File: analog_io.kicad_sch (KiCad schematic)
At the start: 12 parts, among them CN2 MX15EDGRHC-3.5-2*02P-BK01-CU-A, U8 ADS1115IDGS

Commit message: Checkpoint: RA5 base board finished, M.2 shield interconnect defined
Base board (ra5_2022):
- Finalize component placement on ra5_2022.kicad_pcb; next step is routing
- Add STM8S003F3P to bridge the 2 digital inputs / 2 digital outputs onto
  the shared I2C bus (alongside the ADS1115), freeing up M.2 pins
- Wire J1 (M.2 Key-E) to a custom, non-spec-compliant 3.3V pinout: I2C
  (SDA/SCL/ALERT#) on the native pins, M90E32AS SPI reusing the SD/SDIO
  "SPI mode" pin convention (SCLK/MOSI/MISO/CS), PM0/PM1 on VENDOR_DEFINED
  pins, USB-C passthrough, full GND/VDD
- Fix AS0BC21-S40BE-7H footprint: pads 76/77 (shield/ground tabs, not part
  of the 75-pin M.2 spec) remapped onto the GND pin instead of dangling
- Swap the buck inductor (L2) for SLW5040S100MST (C182189): same 10uH,
  lower DCR, 5x5mm footprint to clear a routing constraint
- Remove the unused "Production" KiCad Design Variant and align the
  remaining "Develop" variant's footprints with the defaults -- a
  variant/default footprint mismatch was causing Update PCB from Schematic
  to silently duplicate footprints on every sync
- Clean up 10 further orphaned duplicate footprints left on the PCB from
  earlier design revisions (R11, R12, C14, C16, C17, C18, C29, C31, C32, C35)
- Fix 3D model paths across the shared library to use the RA5_2022_LIB
  environment variable instead of ${KIPRJMOD}, so previews resolve
  correctly from sibling projects too

New sibling project (ra5_shield_modem/):
- MCU + LTE modem card, built to the M.2 Key-E mechanical form factor to
  plug into the base board's J1
- Share the ra5_2022 parts library via sym-lib-table/fp-lib-table
- Add the timonsku/M.2-Card-Footprints submodule as a card-edge template

Co-Authored-By: Claude Sonnet 5 <noreply@anthropic.com>
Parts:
- renumbered C31 to C38, C32 to C39, C35 to C40, D17 to D7, D18 to D8, R57 to R55, R58 to R56, R59 to R57, R60 to R58, R61 to R59, U8 to U12
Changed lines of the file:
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@@
 		(in_pos_files yes)
 		(dnp no)
-		(property "Reference" "C32"
+		(property "Reference" "C39"
 			(at 196.596 76.2 0)
 			(show_name no)
@@
 			(project "ra5_2022"
 				(path "/5cbb1e83-2d68-46fe-9857-942ec50591ae/452b8f5a-797d-4028-91e0-40fe10fe98ae/5bd1a3d1-53b1-46ae-9d95-ca4bdd3c4887"
-					(reference "C32")
+					(reference "C39")
 					(unit 1)
 					(variant
 						(name "Develop")
-					)
-					(variant
-						(name "Production")
 					)
 				)
@@
 		(dnp no)
 		(fields_autoplaced yes)
-		(property "Reference" "#PWR074"
+		(property "Reference" "#PWR080"
 			(at 44.45 59.69 0)
 			(hide yes)
@@
 			(project "ra5_2022"
 				(path "/5cbb1e83-2d68-46fe-9857-942ec50591ae/452b8f5a-797d-4028-91e0-40fe10fe98ae/5bd1a3d1-53b1-46ae-9d95-ca4bdd3c4887"
-					(reference "#PWR074")
+					(reference "#PWR080")
 					(unit 1)
 				)
@@
 		(dnp no)
 		(fields_autoplaced yes)
-		(property "Reference" "R61"
+		(property "Reference" "R59"
 			(at 184.15 104.1399 0)
 			(show_name no)
@@
 			(project "ra5_2022"
 				(path "/5cbb1e83-2d68-46fe-9857-942ec50591ae/452b8f5a-797d-4028-91e0-40fe10fe98ae/5bd1a3d1-53b1-46ae-9d95-ca4bdd3c4887"
-					(reference "R61")
+					(reference "R59")
 					(unit 1)
 					(variant
 						(name "Develop")
-					)
-					(variant
-						(name "Production")
 					)
 				)
@@
 		(dnp no)
 		(fields_autoplaced yes)
-		(property "Reference" "#PWR079"
+		(property "Reference" "#PWR086"
 			(at 128.27 109.22 0)
 			(hide yes)
@@
 			(project "ra5_2022"
 				(path "/5cbb1e83-2d68-46fe-9857-942ec50591ae/452b8f5a-797d-4028-91e0-40fe10fe98ae/5bd1a3d1-53b1-46ae-9d95-ca4bdd3c4887"
-					(reference "#PWR079")
+					(reference "#PWR086")
 					(unit 1)
 				)
@@
 		(dnp no)
 		(fields_autoplaced yes)
-		(property "Reference" "U8"
+		(property "Reference" "U12"
 			(at 130.4133 77.47 0)
 			(show_name no)
@@
 			(project "ra5_2022"
 				(path "/5cbb1e83-2d68-46fe-9857-942ec50591ae/452b8f5a-797d-4028-91e0-40fe10fe98ae/5bd1a3d1-53b1-46ae-9d95-ca4bdd3c4887"
-					(reference "U8")
+					(reference "U12")
 					(unit 1)
 					(variant
 						(name "Develop")
-					)
-					(variant
-						(name "Production")
 					)
 				)
@@
 		(dnp no)
 		(fields_autoplaced yes)
-		(property "Reference" "D17"
+		(property "Reference" "D7"
 			(at 171.7675 62.23 0)
 			(show_name no)
@@
 			(project "ra5_2022"
 				(path "/5cbb1e83-2d68-46fe-9857-942ec50591ae/452b8f5a-797d-4028-91e0-40fe10fe98ae/5bd1a3d1-53b1-46ae-9d95-ca4bdd3c4887"
-					(reference "D17")
+					(reference "D7")
 					(unit 1)
 					(variant
 						(name "Develop")
-					)
-					(variant
-						(name "Production")
 					)
 				)
@@
 		(in_pos_files yes)
 		(dnp no)
-		(property "Reference" "R59"
+		(property "Reference" "R57"
 			(at 66.802 60.96 0)
 			(show_name no)
@@
 			(project "ra5_2022"
 				(path "/5cbb1e83-2d68-46fe-9857-942ec50591ae/452b8f5a-797d-4028-91e0-40fe10fe98ae/5bd1a3d1-53b1-46ae-9d95-ca4bdd3c4887"
-					(reference "R59")
+					(reference "R57")
 					(unit 1)
 					(variant
 						(name "Develop")
-					)
-					(variant
-						(name "Production")
 					)
 				)
@@
 		(dnp no)
 		(fields_autoplaced yes)
-		(property "Reference" "#PWR078"
+		(property "Reference" "#PWR084"
 			(at 76.2 74.93 0)
 			(hide yes)
@@
 			(project "ra5_2022"
 				(path "/5cbb1e83-2d68-46fe-9857-942ec50591ae/452b8f5a-797d-4028-91e0-40fe10fe98ae/5bd1a3d1-53b1-46ae-9d95-ca4bdd3c4887"
-					(reference "#PWR078")
+					(reference "#PWR084")
 					(unit 1)
 				)
@@
 		(dnp no)
 		(fields_autoplaced yes)
-		(property "Reference" "#PWR092"
+		(property "Reference" "#PWR085"
 			(at 128.27 83.82 0)
 			(hide yes)
@@
 			(project "ra5_2022"
 				(path "/5cbb1e83-2d68-46fe-9857-942ec50591ae/452b8f5a-797d-4028-91e0-40fe10fe98ae/5bd1a3d1-53b1-46ae-9d95-ca4bdd3c4887"
-					(reference "#PWR092")
+					(reference "#PWR085")
 					(unit 1)
 				)
@@
 		(in_pos_files yes)
 		(dnp no)
-		(property "Reference" "C35"
+		(property "Reference" "C40"
 			(at 196.596 106.68 0)
 			(show_name no)
@@
 			(project "ra5_2022"
 				(path "/5cbb1e83-2d68-46fe-9857-942ec50591ae/452b8f5a-797d-4028-91e0-40fe10fe98ae/5bd1a3d1-53b1-46ae-9d95-ca4bdd3c4887"
-					(reference "C35")
+					(reference "C40")
 					(unit 1)
 					(variant
 						(name "Develop")
-					)
-					(variant
-						(name "Production")
 					)
 				)
@@
 		(dnp no)
 		(fields_autoplaced yes)
-		(property "Reference" "#PWR076"
+		(property "Reference" "#PWR082"
 			(at 63.5 59.69 0)
 			(hide yes)
@@
 			(project "ra5_2022"
 				(path "/5cbb1e83-2d68-46fe-9857-942ec50591ae/452b8f5a-797d-4028-91e0-40fe10fe98ae/5bd1a3d1-53b1-46ae-9d95-ca4bdd3c4887"
-					(reference "#PWR076")
+					(reference "#PWR082")
 					(unit 1)
 				)
@@
 		(dnp no)
 		(fields_autoplaced yes)
-		(property "Reference" "D18"
+		(property "Reference" "D8"
 			(at 171.7675 92.71 0)
 			(show_name no)
@@
 			(project "ra5_2022"
 				(path "/5cbb1e83-2d68-46fe-9857-942ec50591ae/452b8f5a-797d-4028-91e0-40fe10fe98ae/5bd1a3d1-53b1-46ae-9d95-ca4bdd3c4887"
-					(reference "D18")
+					(reference "D8")
 					(unit 1)
 					(variant
 						(name "Develop")
-					)
-					(variant
-						(name "Production")
 					)
 				)
@@
 						(name "Develop")
 					)
-					(variant
-						(name "Production")
-					)
 				)
 			)
@@
 		(dnp no)
 		(fields_autoplaced yes)
-		(property "Reference" "#PWR075"
+		(property "Reference" "#PWR081"
 			(at 54.61 59.69 0)
 			(hide yes)
@@
 			(project "ra5_2022"
 				(path "/5cbb1e83-2d68-46fe-9857-942ec50591ae/452b8f5a-797d-4028-91e0-40fe10fe98ae/5bd1a3d1-53b1-46ae-9d95-ca4bdd3c4887"
-					(reference "#PWR075")
+					(reference "#PWR081")
 					(unit 1)
 				)
@@
 		(in_pos_files yes)
 		(dnp no)
-		(property "Reference" "R58"
+		(property "Reference" "R56"
 			(at 57.912 60.96 0)
 			(show_name no)
@@
 			(project "ra5_2022"
 				(path "/5cbb1e83-2d68-46fe-9857-942ec50591ae/452b8f5a-797d-4028-91e0-40fe10fe98ae/5bd1a3d1-53b1-46ae-9d95-ca4bdd3c4887"
-					(reference "R58")
+					(reference "R56")
 					(unit 1)
 					(variant
 						(name "Develop")
-					)
-					(variant
-						(name "Production")
 					)
 				)
@@
 		(dnp no)
 		(fields_autoplaced yes)
-		(property "Reference" "#PWR091"
+		(property "Reference" "#PWR087"
 			(at 138.43 104.14 0)
 			(hide yes)
@@
 			(project "ra5_2022"
 				(path "/5cbb1e83-2d68-46fe-9857-942ec50591ae/452b8f5a-797d-4028-91e0-40fe10fe98ae/5bd1a3d1-53b1-46ae-9d95-ca4bdd3c4887"
-					(reference "#PWR091")
+					(reference "#PWR087")
 					(unit 1)
 				)
@@
 		(in_pos_files yes)
 		(dnp no)
-		(property "Reference" "R57"
+		(property "Reference" "R55"
 			(at 47.752 60.96 0)
 			(show_name no)
@@
 			(project "ra5_2022"
 				(path "/5cbb1e83-2d68-46fe-9857-942ec50591ae/452b8f5a-797d-4028-91e0-40fe10fe98ae/5bd1a3d1-53b1-46ae-9d95-ca4bdd3c4887"
-					(reference "R57")
+					(reference "R55")
 					(unit 1)
 					(variant
 						(name "Develop")
-					)
-					(variant
-						(name "Production")
 					)
 				)
@@
 		(dnp no)
 		(fields_autoplaced yes)
-		(property "Reference" "#PWR077"
+		(property "Reference" "#PWR083"
 			(at 76.2 59.69 0)
 			(hide yes)
@@
 			(project "ra5_2022"
 				(path "/5cbb1e83-2d68-46fe-9857-942ec50591ae/452b8f5a-797d-4028-91e0-40fe10fe98ae/5bd1a3d1-53b1-46ae-9d95-ca4bdd3c4887"
-					(reference "#PWR077")
+					(reference "#PWR083")
 					(unit 1)
 				)
@@
 		(in_pos_files yes)
 		(dnp no)
-		(property "Reference" "C31"
+		(property "Reference" "C38"
 			(at 79.756 63.5 0)
 			(show_name no)
@@
 			(project "ra5_2022"
 				(path "/5cbb1e83-2d68-46fe-9857-942ec50591ae/452b8f5a-797d-4028-91e0-40fe10fe98ae/5bd1a3d1-53b1-46ae-9d95-ca4bdd3c4887"
-					(reference "C31")
+					(reference "C38")
 					(unit 1)
 					(variant
 						(name "Develop")
-					)
-					(variant
-						(name "Production")
 					)
 				)
@@
 		(dnp no)
 		(fields_autoplaced yes)
-		(property "Reference" "R60"
+		(property "Reference" "R58"
 			(at 184.15 73.6599 0)
 			(show_name no)
@@
 			(project "ra5_2022"
 				(path "/5cbb1e83-2d68-46fe-9857-942ec50591ae/452b8f5a-797d-4028-91e0-40fe10fe98ae/5bd1a3d1-53b1-46ae-9d95-ca4bdd3c4887"
-					(reference "R60")
+					(reference "R58")
 					(unit 1)
 					(variant
 						(name "Develop")
 					)
-					(variant
-						(name "Production")
-					)
-				)
+				)

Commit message: Migra componentes das bibliotecas LCSC locais para pecas JLCPCB
Troca os part numbers para casar com o estoque da JLCPCB e com o
catalogo PCBA Basic, eliminando a biblioteca local que era importada
via easyeda2kicad.

- Remove libraries/ (simbolos, footprints e modelos 3D importados) e o
  script import_lcsc_component.sh
- Adiciona o plugin JLCPCB (jlcpcb/project.db) e os scripts auxiliares
  fix_jlcpcb_tools_deps.sh e generate_ibom.sh
- Atualiza as cinco folhas do esquematico, o PCB e as regras de projeto

O PCB fica em estado intermediario: os componentes novos ainda precisam
ser reposicionados e as trilhas refeitas.

Co-Authored-By: Claude Opus 5 (1M context) <noreply@anthropic.com>
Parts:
- C38, C39, C40: footprint Capacitor_SMD:C_0201_0603Metric -> Capacitor_SMD:C_0402_1005Metric; JLCPCB Part # (none) -> C1525; LCSC Part # C7393837 -> (none); MPN TCC0201X7R104K100ZT -> CL05B104KO5NNNC
- CN2: JLCPCB Part # (none) -> C49142488; LCSC Part # C49142488 -> (none)
- D7, D8: value SD103AWS -> 1N5819WS; JLCPCB Part # (none) -> C191023; LCSC Part # C22438316 -> (none); MPN SD103AWS -> 1N5819WS
- R55, R56, R57: JLCPCB Part # (none) -> C25744; LCSC Part # C102759 -> (none); MPN RTT02103JTH -> 0402WGF1002TCE
- R58, R59: JLCPCB Part # (none) -> C17901; LCSC Part # C54974076 -> (none); MPN CRF1206Q1000PN -> 1206W4F1000T5E
- U12: JLCPCB Part # (none) -> C37593; LCSC Part # C37593 -> (none)
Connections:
- net AIN0: now also C39.1, D8.1 (K); no longer C39.2, D7.1 (K)
- net AIN1: now also C39.2; no longer C39.1
- net AIN1+: now also D8.2 (A); no longer D7.2 (A)
- net AIN2: now also C40.1, D7.1 (K); no longer C40.2, D8.1 (K)
- net AIN2+: now also D7.2 (A); no longer D8.2 (A)
- net AIN2-: now also C40.2; no longer C40.1
- net GND: now also C38.2; no longer C38.1
- net SDA: no longer R56.1
- net VDD: now also C38.1; no longer C38.2, R56.2

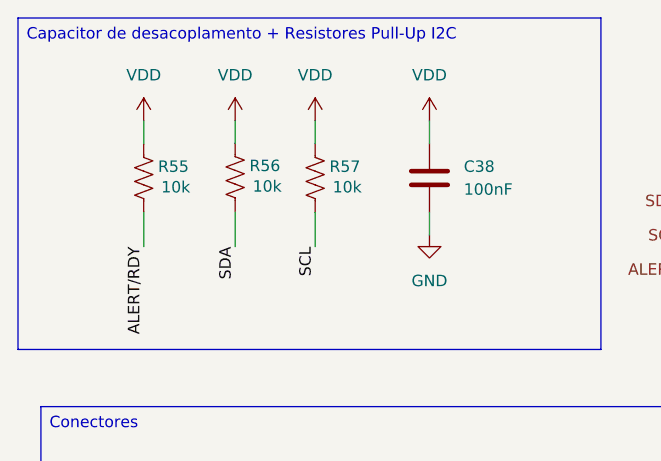
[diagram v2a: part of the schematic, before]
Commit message: Reintroduz biblioteca local ra5_2022 e atualiza layout/esquematicos
Volta a usar simbolos, footprints e modelos 3D importados via
easyeda2kicad (libraries/) em vez das pecas basicas JLCPCB adotadas no
commit anterior, alem de atualizar o roteamento/posicionamento no PCB
e as cinco folhas do esquematico.

Co-Authored-By: Claude Sonnet 5 <noreply@anthropic.com>
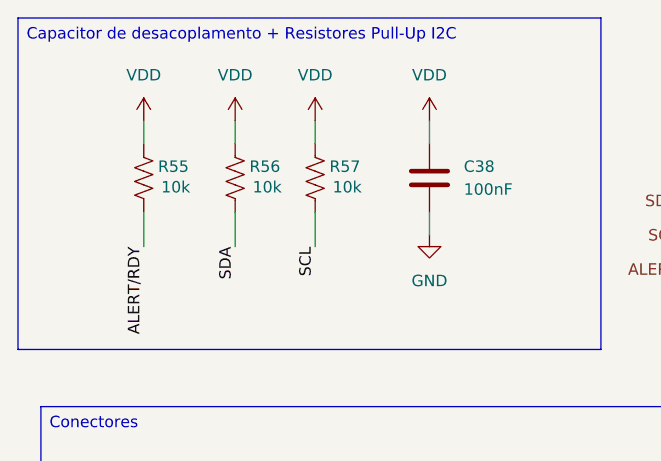
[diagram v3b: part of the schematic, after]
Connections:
- net SDA: now also R56.1
- net VDD: now also R56.2
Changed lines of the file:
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@@
 	(symbol
 		(lib_id "Device:R_US")
-		(at 54.6089 62.1424 180)
+		(at 54.61 62.23 180)
 		(unit 1)
 		(body_style 1)
@@
 		(dnp no)
 		(property "Reference" "R56"
-			(at 57.9109 60.8724 0)
+			(at 57.912 60.96 0)
 			(show_name no)
 			(do_not_autoplace no)
@@
 		)
 		(property "Value" "10k"
-			(at 58.1649 63.1584 0)
+			(at 58.166 63.246 0)
 			(show_name no)
 			(do_not_autoplace no)
@@
 		)
 		(property "Footprint" "Resistor_SMD:R_0402_1005Metric"
-			(at 54.6089 62.1424 0)
+			(at 54.61 62.23 0)
 			(hide yes)
 			(show_name no)
@@
 		)
 		(property "Datasheet" "https://jlc-prod-smt.oss-eu-central-1.aliyuncs.com/smtDataManualFile/8556212101494185984-C25744.pdf?response-content-disposition=attachment%3B%20filename%3DC25744.pdf%3B%20filename%2A%3DUTF-8%27%27C25744.pdf&x-oss-date=20260806T132247Z&x-oss-expires=1800&x-oss-security-token=CAISgAN1q6Ft5B2yfSjIr5vRCez81Ix7jordMUX8hWIHT%2B55vKfcqDz2IHhMdHJsAOodtv0%2FmmhT6PkclqRLcbhpcmfjV%2BZHzLB8qbMSmV5U4J7b16cNrbH4M4H6aXeirtuwDsz9SNTCALjPD3nPii50x5bjaDymRCbLGJaViJlhHLN1Ow6jdmhpCctxLAlvo9NgFxm3D%2Fu2NQPwiWf9FVdhvhEG6Vly8qOi2MaRmFy8yFTx0b0SvJ%2BjYMrmPctoN9JnSdC5mfdzau3a1TJ84gRD0a5wkaVA1zbDs5bfISEIuUzebreLqY03dV4mOvdqIcMe8qigz88fk%2FfIioH6xyxKOexoSCnFTOiiupCcQLPyao9jLu6iayqViY7QaIOTqQohZmkAMwVOasAsI3Ngh4zF97Qt0cVNkXO9gWfLI8DtuMleWkqsV8sOKnSgc5lCkRRYwGs1287ugXlSQzo890KPDAEovaKCnZ2ZSfh7Y4sNknI6i%2Bfc2Se2MIkIPW%2FsfaKWD5sagAEqVCQAL2QfAkO1%2BFQWQNgiyzdWFNst5LvhtKwzmogNxZ0zScnTgMdQHsK7xeDbh4uAh3U9G%2BurY3qhE2Ms6P52SHhCkPtqK1%2FrMZDol1gdFGu2FkajMNNLWkrjzopG2cg0YncyekG4N26y4k3hyApM7Y5VgCcb%2B2%2BIYOkDJbJJZiAA&x-oss-signature-version=OSS4-HMAC-SHA256&x-oss-credential=STS.NXdBVH9SZ9H63cMabRCaUSbwJ%2F20260806%2Feu-central-1%2Foss%2Faliyun_v4_request&x-oss-signature=18a9af57d3a21a3be94a75ea6d5e0857f607d3389e658fe9e592a63e7ed7c757"
-			(at 54.6089 62.1424 0)
+			(at 54.61 62.23 0)
 			(hide yes)
 			(show_name no)
@@
 		)
 		(property "Description" "-55℃~+155℃ 10kΩ 50V 62.5mW Thick Film Resistor ±1% ±100ppm/℃ 0402 Chip Resistor - Surface Mount ROHS"
-			(at 54.6089 62.1424 0)
+			(at 54.61 62.23 0)
 			(hide yes)
 			(show_name no)
@@
 		)
 		(property "MPN" "0402WGF1002TCE"
-			(at 54.6089 62.1424 0)
+			(at 54.61 62.23 0)
 			(hide yes)
 			(show_name no)
@@
 		)
 		(property "JLCPCB Part #" "C25744"
-			(at 54.6089 62.1424 0)
+			(at 54.61 62.23 0)
 			(hide yes)
 			(show_name no)
@@
 		)
 		(property "LCSC Part" ""
-			(at 54.6089 62.1424 0)
+			(at 54.61 62.23 0)
 			(hide yes)
 			(show_name no)
@@
 		)
 		(property "KLC_S3.3" ""
-			(at 54.6089 62.1424 0)
+			(at 54.61 62.23 0)
 			(hide yes)
 			(show_name no)
@@
 		)
 		(property "KLC_S4.1" ""
-			(at 54.6089 62.1424 0)
+			(at 54.61 62.23 0)
 			(hide yes)
 			(show_name no)
@@
 		)
 		(property "LCSC Part #" ""
-			(at 54.6089 62.1424 0)
+			(at 54.61 62.23 0)
 			(hide yes)
 			(show_name no)
